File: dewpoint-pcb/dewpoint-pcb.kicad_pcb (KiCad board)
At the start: 2 copper layers, 93.8 x 98 mm, 25 parts, among them J1 Power Terminal, J2 Relais Connector, J3 Sensor Outside, J4 Sensor Inside, J5 Display Connector, J6 Reset Button, J7 3-way On/Auto/Off-Switch

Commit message: v1.0, gerber.zip
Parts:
- removed the ? at (58.4, 84.0)
- removed the ? at (69.2, 84.0)
- moved J6 49.0 mm to (48.3, 57.7), turned to -90 degrees
- moved J3 22.8 mm to (96.4, 105.5)
- moved J4 22.8 mm to (113.4, 105.5)
- moved J7 22.8 mm to (79.2, 105.5)
- moved C2 11.6 mm to (90.9, 47.6), turned to 180 degrees
- moved C1 7.31 mm to (67.8, 45.5)
- moved J1 7.11 mm to (48.3, 46.2)
- moved J2 2.59 mm to (50.6, 74.3)
- moved J5 2.56 mm to (135.1, 101.6)
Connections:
- J2 pad 1: Relais -> GND
- J2 pad 3: GND -> Relais
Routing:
- net +5V: track 0.00 -> 190.6 mm, vias 0 -> 1
- net SCL: track 0.00 -> 120.4 mm, vias 0 -> 2
- net SDA: track 0.00 -> 115.3 mm, vias 0 -> 2
- net DHT Inside: track 0.00 -> 78.0 mm, vias 0 -> 3
- net DHT Outside: track 0.00 -> 75.4 mm, vias 0 -> 3
- net Relais: track 0.00 -> 71.3 mm, vias 0 -> 2
- net Net-(J7-Pad2): track 0.00 -> 57.0 mm, vias 0 -> 1
- net Reset: track 0.00 -> 49.0 mm, vias 0 -> 1
- added copper zone on B.Cu, net GND
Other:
- board size 93.8 x 98 mm -> 93.8 x 97.5 mm
- board text added: "Power"
- board text added: "Relais"
- board text removed: "Power Terminal"
- board text removed: "Relais Connector"

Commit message: updated pcb gerber
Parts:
- moved J6 1.06 mm to (48.3, 58.7)
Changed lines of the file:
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@@
       (effects (font (size 1 1) (thickness 0.15)))
     )
-    (fp_text value "Relais Connector" (at -4.38 7.85 90) (layer "F.Fab")
+    (fp_text value "Relais Connector" (at -4.38 7.85 90) (layer "F.Fab") hide
       (effects (font (size 1 1) (thickness 0.15)))
     )
@@
   )
   (footprint "TerminalBlock_Phoenix:TerminalBlock_Phoenix_MKDS-1,5-2_1x02_P5.00mm_Horizontal" (layer "F.Cu")
-    (at 48.26 57.658 -90)
+    (at 48.26 58.714 -90)
     (descr "Terminal Block Phoenix MKDS-1,5-2, 2 pins, pitch 5mm, size 10x9.8mm^2, drill diamater 1.3mm, pad diameter 2.6mm, see http://www.farnell.com/datasheets/100425.pdf, script-generated using https://github.com/pointhi/kicad-footprint-generator/scripts/TerminalBlock_Phoenix")
     (tags "THT Terminal Block Phoenix MKDS-1,5-2 pitch 5mm size 10x9.8mm^2 drill 1.3mm pad 2.6mm")
@@
     (effects (font (size 1 1) (thickness 0.15)))
   )
-  (gr_text "Reset" (at 56.134 62.484) (layer "F.SilkS")
+  (gr_text "Reset" (at 55.88 63.754) (layer "F.SilkS")
     (effects (font (size 1 1) (thickness 0.15)))
   )
@@
     (effects (font (size 1 1) (thickness 0.15)))
   )
-  (gr_text "GND" (at 55.626 57.404) (layer "F.SilkS")
+  (gr_text "GND" (at 55.372 58.674) (layer "F.SilkS")
     (effects (font (size 1 1) (thickness 0.15)))
   )
@@
     (effects (font (size 1 1) (thickness 0.15)))
   )
-  (gr_text "S" (at 50.165 69.469 270) (layer "F.SilkS")
-    (effects (font (size 1 1) (thickness 0.15)))
-  )
-  (gr_text "Reset Button" (at 59.436 59.436 270) (layer "F.SilkS")
+  (gr_text "S" (at 55.372 71.882 270) (layer "F.SilkS")
+    (effects (font (size 1 1) (thickness 0.15)))
+  )
+  (gr_text "Reset Button" (at 59.182 61.468 270) (layer "F.SilkS")
     (effects (font (size 1 1) (thickness 0.15)))
   )
@@
     (effects (font (size 1 1) (thickness 0.15)))
   )
-  (gr_text "Relais" (at 52.959 66.675) (layer "F.SilkS")
+  (gr_text "Relais" (at 52.832 68.326) (layer "F.SilkS")
     (effects (font (size 1 1) (thickness 0.15)))
   )
@@
     (effects (font (size 1 1) (thickness 0.15)))
   )
-  (gr_text "5V" (at 52.832 69.088 90) (layer "F.SilkS")
+  (gr_text "5V" (at 53.086 71.374 90) (layer "F.SilkS")
     (effects (font (size 1 1) (thickness 0.15)))
   )
@@
     (effects (font (size 1 1) (thickness 0.15)))
   )
-  (gr_text "GND" (at 55.372 68.58 90) (layer "F.SilkS")
+  (gr_text "GND" (at 50.292 70.866 90) (layer "F.SilkS")
     (effects (font (size 1 1) (thickness 0.15)))
   )
@@
   (segment (start 132.08 60.96) (end 132.08 106.172) (width 0.6) (layer "B.Cu") (net 24))
   (segment (start 101.19 64.164) (end 101.19 53.33) (width 0.6) (layer "B.Cu") (net 24))
-  (segment (start 52.752 58.166) (end 88.138 58.166) (width 0.6) (layer "F.Cu") (net 28))
-  (segment (start 48.26 62.658) (end 52.752 58.166) (width 0.6) (layer "F.Cu") (net 28))
   (segment (start 90.17 58.166) (end 90.932 57.404) (width 0.6) (layer "F.Cu") (net 28))
-  (segment (start 88.138 58.166) (end 90.17 58.166) (width 0.6) (layer "F.Cu") (net 28))
+  (segment (start 48.26 63.714) (end 53.808 58.166) (width 0.6) (layer "F.Cu") (net 28))
+  (segment (start 53.808 58.166) (end 90.17 58.166) (width 0.6) (layer "F.Cu") (net 28))
   (via (at 90.932 57.404) (size 0.8) (drill 0.4) (layers "F.Cu" "B.Cu") (net 28))
   (segment (start 90.932 53.428) (end 91.03 53.33) (width 0.6) (layer "B.Cu") (net 28))

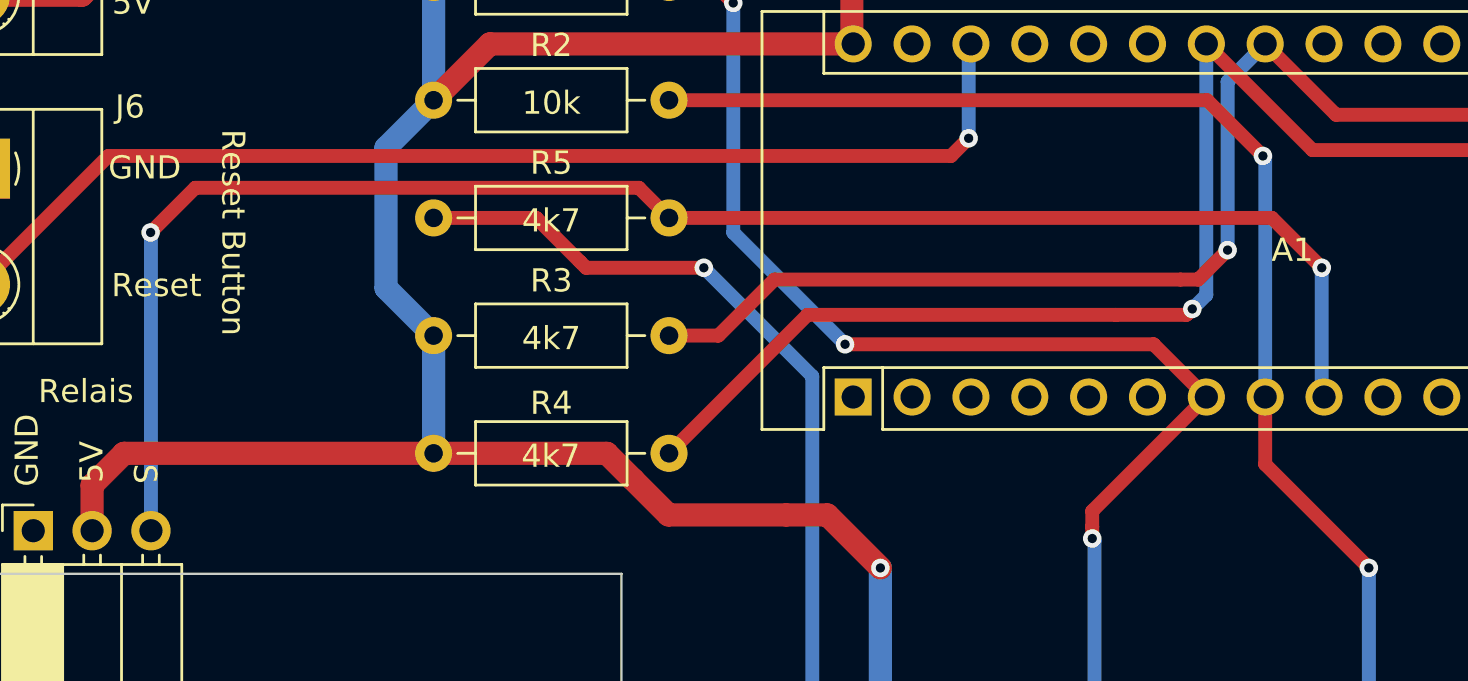
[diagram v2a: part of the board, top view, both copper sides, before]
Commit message: Correction, Relais switch wasn't connected correctly.
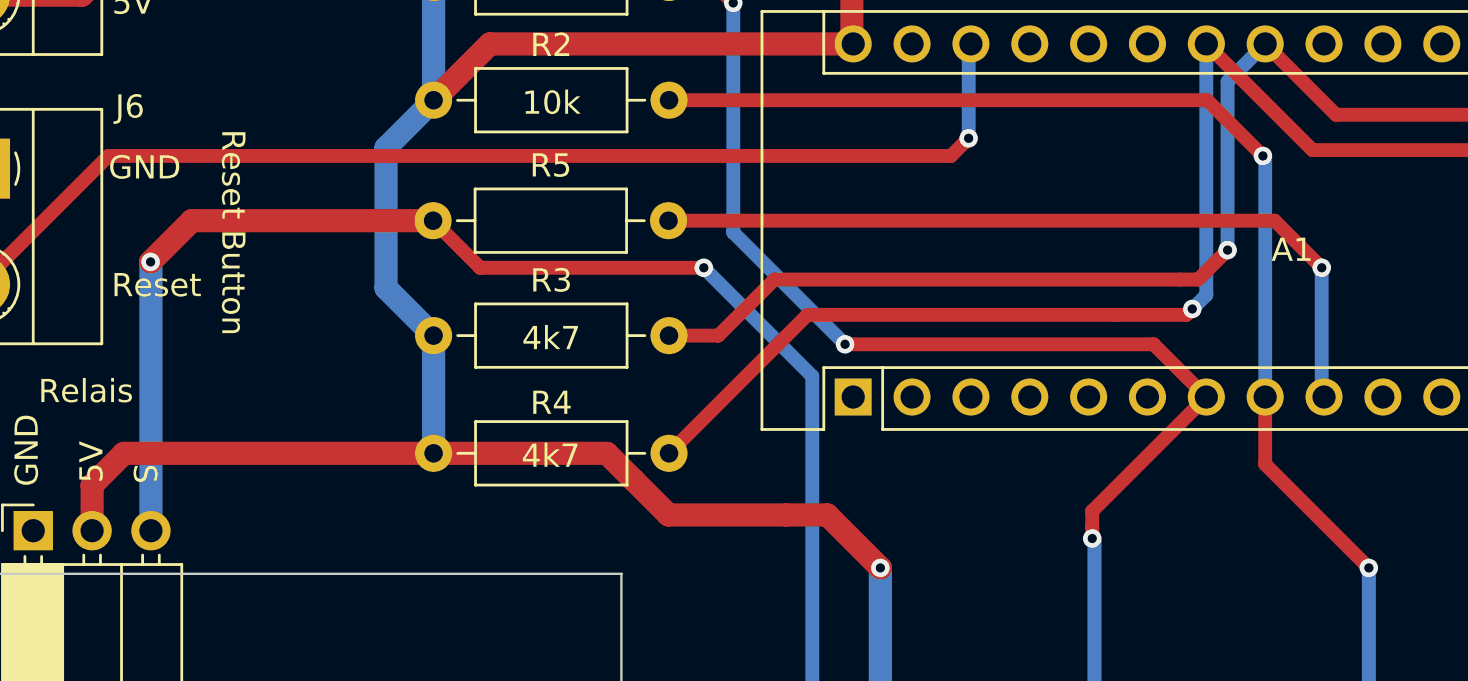
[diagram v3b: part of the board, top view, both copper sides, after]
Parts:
- moved R5 0.12 mm to (67.8, 61.0)
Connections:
- A1 pad 9: Relais -> Net-(A1-Pad9)
- J7 pad 2: Net-(J7-Pad2) -> Relais
- R5 pad 1: Net-(J7-Pad2) -> Relais
- R5 pad 2: Relais -> Net-(A1-Pad9)
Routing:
- net Net-(J7-Pad2): track 57.0 -> 0.00 mm, vias 1 -> 0
- net Net-(A1-Pad9): track 0.00 -> 34.7 mm, vias 0 -> 1
- net Relais: track 71.3 -> 81.5 mm
